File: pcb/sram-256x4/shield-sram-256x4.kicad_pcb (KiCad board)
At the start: 4 copper layers, 100 x 100 mm, 31 parts, among them J1 QSH-060-01-L-D-A, J2 QSH-060-01-L-D-A, U1 IS61WV25616-10TLI, U2 IS61WV25616-10TLI, U3 IS61WV25616-10TLI, U4 IS61WV25616-10TLI

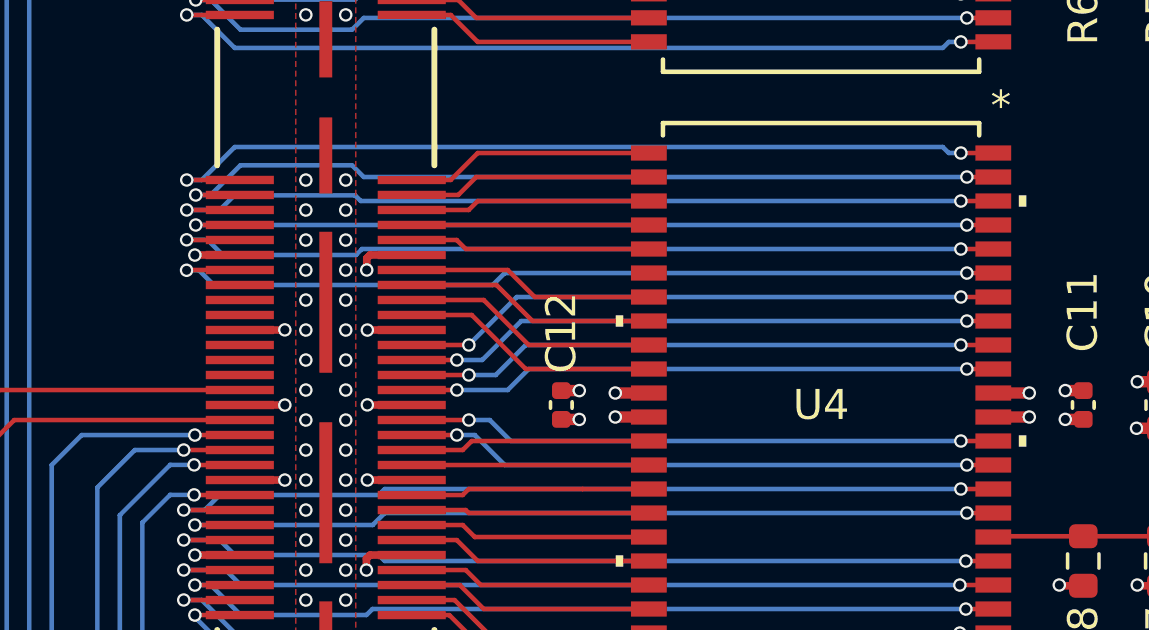
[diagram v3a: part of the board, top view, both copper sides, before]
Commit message: [sram] attempted D signal issue work around
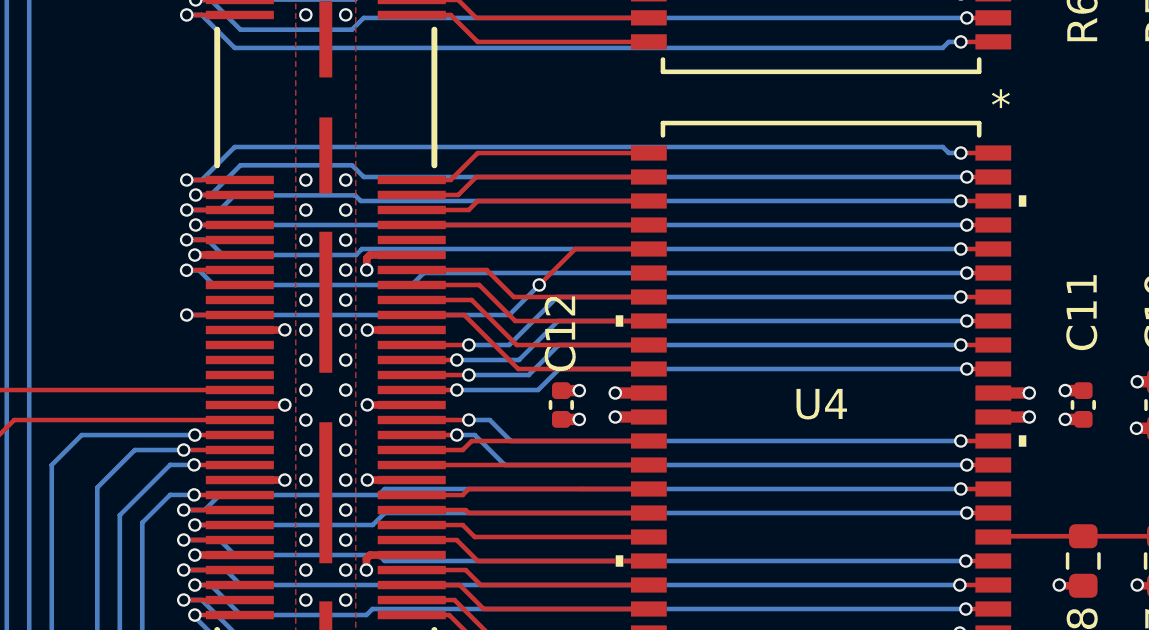
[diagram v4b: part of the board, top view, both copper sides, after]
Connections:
- U4 pad 27: D10 -> D17
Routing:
- net D17: track 0.00 -> 18.2 mm, vias 0 -> 2
- net D10: track 8.03 -> 0.00 mm
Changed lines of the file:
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@@
 		(allow_soldermask_bridges_in_footprints no)
 		(tenting front back)
-		(grid_origin 39.034899 105.54905)
+		(grid_origin 104.267668 57.54405)
 		(pcbplotparams
 			(layerselection 0x00000000_00000000_55555555_5755f5ff)
@@
 			(size 1.1938 0.508)
 			(layers "F.Cu" "F.Mask" "F.Paste")
-			(net 116 "D10")
+			(net 154 "D17")
 			(pinfunction "A14")
 			(pintype "input")
@@
 	)
 	(segment
-		(start 107.767117 58.4449)
-		(end 122.571868 58.4449)
+		(start 106.171869 60.0449)
+		(end 107.516818 60.0449)
 		(width 0.1524)
 		(layer "B.Cu")
@@
 	)
 	(segment
-		(start 106.171868 60.040149)
-		(end 107.767117 58.4449)
+		(start 107.516818 60.0449)
+		(end 109.116818 58.4449)
 		(width 0.1524)
 		(layer "B.Cu")
@@
 	)
 	(segment
-		(start 106.171869 60.0449)
-		(end 106.171868 60.040149)
+		(start 109.116818 58.4449)
+		(end 122.571868 58.4449)
 		(width 0.1524)
 		(layer "B.Cu")
@@
 	)
 	(segment
-		(start 108.167668 60.844349)
+		(start 109.179944 60.844349)
 		(end 122.771317 60.844349)
 		(width 0.1524)
@@
 	)
 	(segment
-		(start 107.467117 61.5449)
-		(end 108.167668 60.844349)
+		(start 122.771317 60.844349)
+		(end 122.771868 60.8449)
 		(width 0.1524)
 		(layer "B.Cu")
@@
 	)
 	(segment
-		(start 122.771317 60.844349)
-		(end 122.771868 60.8449)
+		(start 105.771868 61.5449)
+		(end 108.479393 61.5449)
 		(width 0.1524)
 		(layer "B.Cu")
@@
 	)
 	(segment
-		(start 105.771868 61.5449)
-		(end 107.467117 61.5449)
+		(start 108.479393 61.5449)
+		(end 109.179944 60.844349)
 		(width 0.1524)
 		(layer "B.Cu")
@@
 	)
 	(segment
-		(start 106.068221 56.844903)
-		(end 112.171868 56.844902)
-		(width 0.1524)
-		(layer "F.Cu")
-		(net 116)
-	)
-	(segment
-		(start 105.767167 56.543849)
-		(end 106.068221 56.844903)
-		(width 0.1524)
-		(layer "F.Cu")
-		(net 116)
-	)
-	(segment
-		(start 104.267668 56.543849)
-		(end 105.767167 56.543849)
-		(width 0.1524)
-		(layer "F.Cu")
-		(net 116)
-	)
-	(segment
 		(start 107.269515 35.539953)
 		(end 112.171868 35.539953)
@@
 	)
 	(segment
-		(start 104.267668 58.044149)
-		(end 107.092468 58.044149)
+		(start 106.517767 58.044149)
+		(end 107.718518 59.2449)
 		(width 0.1524)
 		(layer "F.Cu")
@@
 	)
 	(segment
-		(start 108.293219 59.2449)
+		(start 107.718518 59.2449)
 		(end 112.171868 59.2449)
 		(width 0.1524)
@@
 	)
 	(segment
-		(start 107.092468 58.044149)
-		(end 108.293219 59.2449)
+		(start 104.267668 58.044149)
+		(end 106.517767 58.044149)
 		(width 0.1524)
 		(layer "F.Cu")
@@
 	)
 	(segment
-		(start 108.068218 60.844899)
-		(end 106.267668 59.044349)
+		(start 107.818517 60.844899)
+		(end 106.017967 59.044349)
 		(width 0.1524)
 		(layer "F.Cu")
@@
 	)
 	(segment
-		(start 112.171868 60.844899)
-		(end 108.068218 60.844899)
+		(start 106.017967 59.044349)
+		(end 104.267667 59.044349)
 		(width 0.1524)
 		(layer "F.Cu")
@@
 	)
 	(segment
-		(start 106.267668 59.044349)
-		(end 104.267667 59.044349)
+		(start 112.171868 60.844899)
+		(end 107.818517 60.844899)
 		(width 0.1524)
 		(layer "F.Cu")
@@
 	)
 	(segment
+		(start 98.537668 59.04435)
+		(end 96.767968 59.04435)
+		(width 0.1524)
+		(layer "F.Cu")
+		(net 154)
+	)
+	(segment
+		(start 111.81852 56.844902)
+		(end 111.767668 56.79405)
+		(width 0.1524)
+		(layer "F.Cu")
+		(net 154)
+	)
+	(segment
+		(start 112.171868 56.844902)
+		(end 109.716816 56.844902)
+		(width 0.1524)
+		(layer "F.Cu")
+		(net 154)
+	)
+	(segment
+		(start 109.716816 56.844902)
+		(end 108.517668 58.04405)
+		(width 0.1524)
+		(layer "F.Cu")
+		(net 154)
+	)
+	(via
+		(at 96.767968 59.04435)
+		(size 0.45)
+		(drill 0.3)
+		(layers "F.Cu" "B.Cu")
+		(net 154)
+	)
+	(via
+		(at 108.517668 58.04405)
+		(size 0.45)
+		(drill 0.3)
+		(layers "F.Cu" "B.Cu")
+		(net 154)
+	)
+	(segment
+		(start 96.767968 59.04435)
+		(end 107.517368 59.04435)
+		(width 0.1524)
+		(layer "B.Cu")
+		(net 154)
+	)
+	(segment
+		(start 107.517368 59.04435)
+		(end 108.517668 58.04405)
+		(width 0.1524)
+		(layer "B.Cu")
+		(net 154)
+	)
+	(segment
 		(start 104.267668 47.54305)
 		(end 112.170716 47.54305)
@@
 	)
 	(segment
-		(start 107.917117 59.244899)
-		(end 122.771868 59.2449)
+		(start 105.771868 60.5449)
+		(end 107.841818 60.5449)
 		(width 0.1524)
 		(layer "B.Cu")
@@
 	)
 	(segment
-		(start 105.771868 60.5449)
-		(end 106.617117 60.5449)
+		(start 109.141818 59.2449)
+		(end 122.771868 59.2449)
 		(width 0.1524)
 		(layer "B.Cu")
@@
 	)
 	(segment
-		(start 106.617117 60.5449)
-		(end 107.917117 59.244899)
+		(start 107.841818 60.5449)
+		(end 109.141818 59.2449)
 		(width 0.1524)
 		(layer "B.Cu")
@@
 	)
 	(segment
-		(start 104.267667 58.544249)
-		(end 106.667568 58.544249)
+		(start 107.768518 60.0449)
+		(end 112.171868 60.0449)
 		(width 0.1524)
 		(layer "F.Cu")
@@
 	)
 	(segment
-		(start 108.168219 60.0449)
-		(end 112.171868 60.0449)
+		(start 106.267867 58.544249)
+		(end 107.768518 60.0449)
 		(width 0.1524)
 		(layer "F.Cu")
@@
 	)
 	(segment
-		(start 106.667568 58.544249)
-		(end 108.168219 60.0449)
+		(start 104.267667 58.544249)
+		(end 106.267867 58.544249)
 		(width 0.1524)
 		(layer "F.Cu")
@@
 	)
 	(segment
-		(start 97.176877 57.553559)
-		(end 97.667668 58.044349)
+		(start 104.667668 57.644349)
+		(end 122.769918 57.644349)
 		(width 0.1524)
 		(layer "B.Cu")
@@
 	)
 	(segment
-		(start 96.762676 57.553558)
-		(end 97.176877 57.553559)
+		(start 122.769918 57.644349)
+		(end 122.771868 57.646299)
 		(width 0.1524)
 		(layer "B.Cu")
@@
 	)
 	(segment
-		(start 97.667668 58.044349)
-		(end 106.967668 58.044349)
+		(start 97.176877 57.553559)
+		(end 97.667668 58.044349)
 		(width 0.1524)
 		(layer "B.Cu")
@@
 	)
 	(segment
-		(start 106.967668 58.044349)
-		(end 107.367668 57.644349)
+		(start 104.267668 58.044349)
+		(end 104.667668 57.644349)
 		(width 0.1524)
 		(layer "B.Cu")
@@
 	)
 	(segment
-		(start 107.369618 57.646299)
-		(end 122.771868 57.646299)
+		(start 97.667668 58.044349)
+		(end 104.267668 58.044349)
 		(width 0.1524)
 		(layer "B.Cu")
@@
 	)
 	(segment
-		(start 107.367668 57.644349)
-		(end 107.369618 57.646299)
+		(start 96.762676 57.553558)
+		(end 97.176877 57.553559)
 		(width 0.1524)
 		(layer "B.Cu")
@@
 	)
 	(segment
-		(start 107.067117 61.0449)
-		(end 108.067117 60.0449)
+		(start 106.171868 61.0449)
+		(end 108.166818 61.0449)
 		(width 0.1524)
 		(layer "B.Cu")
@@
 	)
 	(segment
-		(start 108.067117 60.0449)
-		(end 122.571868 60.0449)
+		(start 108.166818 61.0449)
+		(end 109.166818 60.0449)
 		(width 0.1524)
 		(layer "B.Cu")
@@
 	)
 	(segment
-		(start 106.171868 61.0449)
-		(end 107.067117 61.0449)
+		(start 109.166818 60.0449)
+		(end 122.571868 60.0449)
 		(width 0.1524)
 		(layer "B.Cu")
@@
 	)
 	(segment
-		(start 107.467368 57.544049)
-		(end 108.36822 58.444901)
+		(start 106.767667 57.544049)
+		(end 107.668519 58.444901)
 		(width 0.1524)
 		(layer "F.Cu")
@@
 	(segment
 		(start 104.267668 57.544049)
-		(end 107.467368 57.544049)
+		(end 106.767667 57.544049)
 		(width 0.1524)
 		(layer "F.Cu")
@@
 	)
 	(segment
-		(start 108.36822 58.444901)
+		(start 107.668519 58.444901)
 		(end 112.171868 58.444901)
 		(width 0.1524)
